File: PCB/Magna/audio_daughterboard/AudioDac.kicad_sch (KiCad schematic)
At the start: 44 parts, among them U401 NE5532, U403 PCM1789

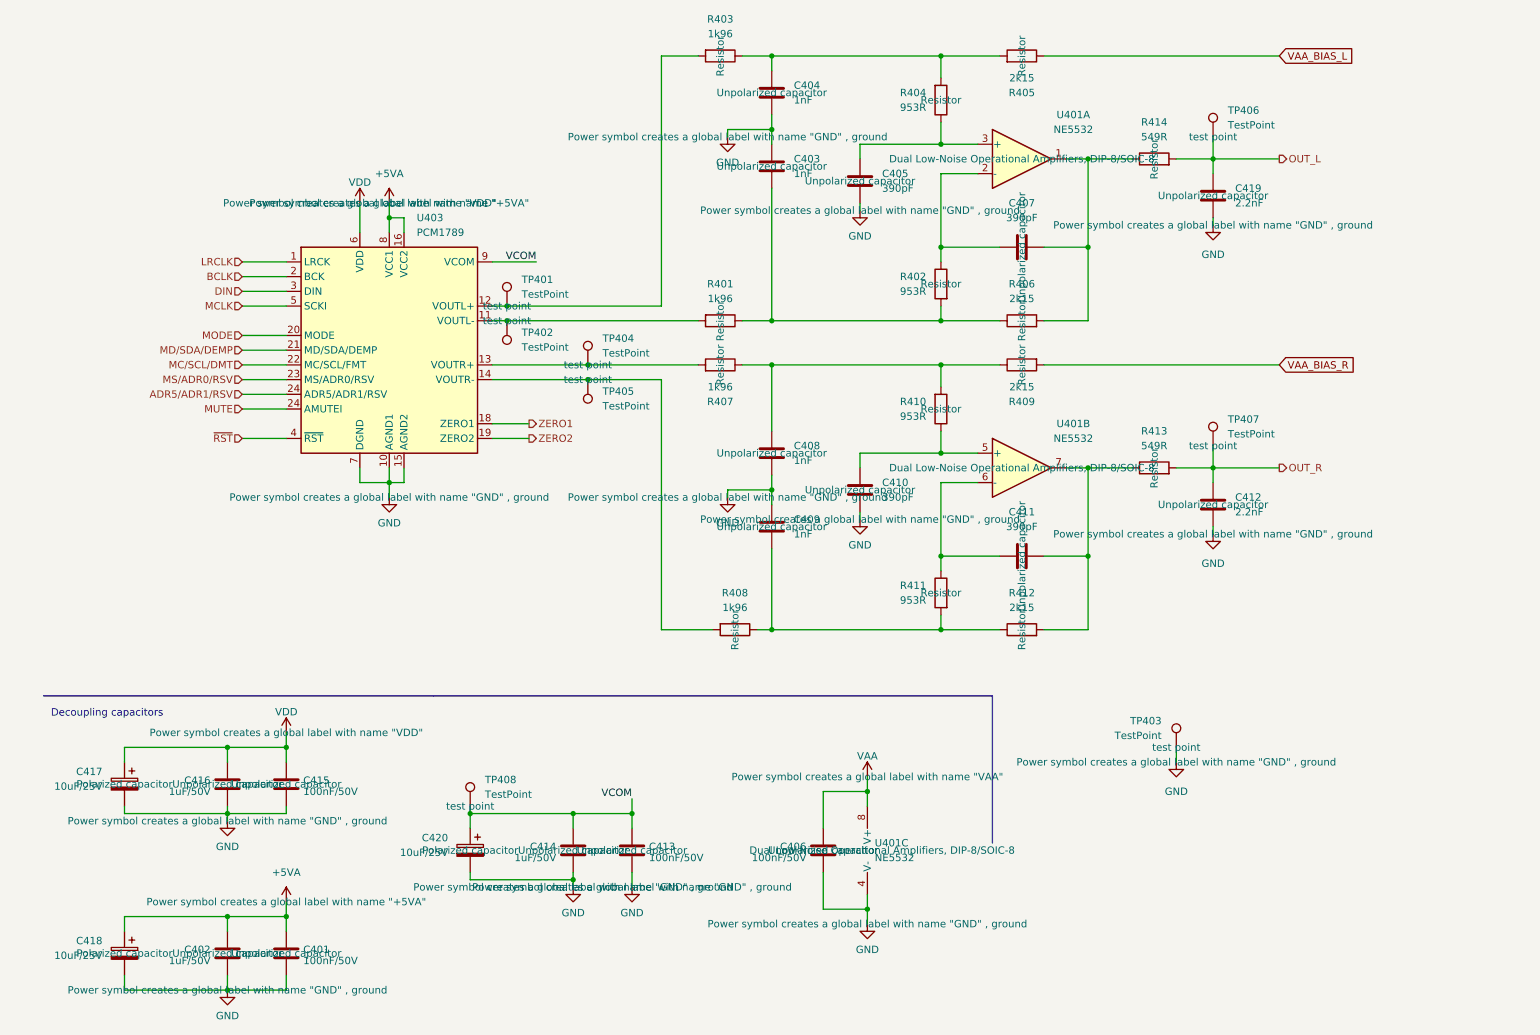
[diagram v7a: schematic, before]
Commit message: Update schematics to Kicad 9
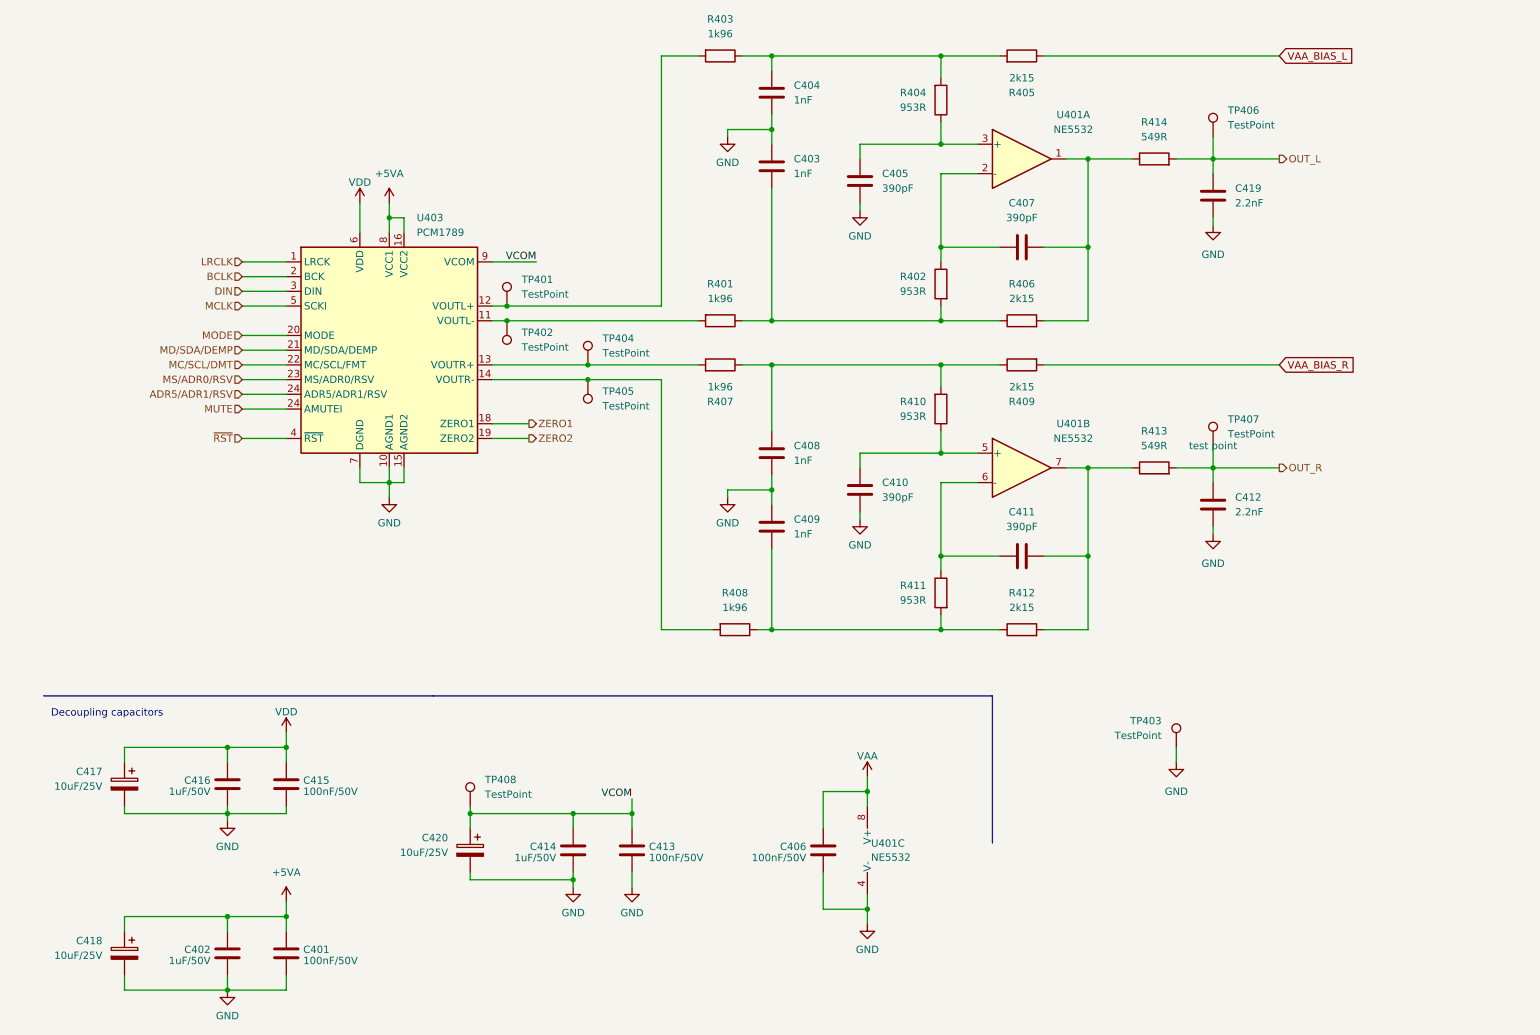
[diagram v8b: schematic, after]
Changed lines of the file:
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@@
 					(size 1.27 1.27)
 				)
+				(hide yes)
 			)
 		)
@@
 					(size 1.27 1.27)
 				)
+				(hide yes)
 			)
 		)
@@
 					(size 1.27 1.27)
 				)
+				(hide yes)
 			)
 		)
@@
 					(size 1.27 1.27)
 				)
+				(hide yes)
 			)
 		)
@@
 					(size 1.27 1.27)
 				)
+				(hide yes)
 			)
 		)
@@
 					(size 1.27 1.27)
 				)
+				(hide yes)
 			)
 		)
@@
 					(size 1.27 1.27)
 				)
+				(hide yes)
 			)
 		)
@@
 					(size 1.27 1.27)
 				)
+				(hide yes)
 			)
 		)
@@
 					(size 1.27 1.27)
 				)
+				(hide yes)
 			)
 		)
@@
 					(size 1.27 1.27)
 				)
+				(hide yes)
 			)
 		)
@@
 					(size 1.27 1.27)
 				)
+				(hide yes)
 			)
 		)
@@
 					(size 1.27 1.27)
 				)
+				(hide yes)
 			)
 		)
@@
 					(size 1.27 1.27)
 				)
+				(hide yes)
 			)
 		)
@@
 					(size 1.27 1.27)
 				)
+				(hide yes)
 			)
 		)
@@
 					(size 1.27 1.27)
 				)
+				(hide yes)
 			)
 		)
@@
 					(size 1.27 1.27)
 				)
+				(hide yes)
 			)
 		)
@@
 					(size 1.27 1.27)
 				)
+				(hide yes)
 			)
 		)
@@
 					(size 1.27 1.27)
 				)
+				(hide yes)
 			)
 		)
@@
 					(size 1.27 1.27)
 				)
+				(hide yes)
 			)
 		)
@@
 					(size 1.27 1.27)
 				)
+				(hide yes)
 			)
 		)
@@
 					(size 1.27 1.27)
 				)
+				(hide yes)
 			)
 		)
@@
 					(size 1.27 1.27)
 				)
+				(hide yes)
 			)
 		)
@@
 					(size 1.27 1.27)
 				)
+				(hide yes)
 			)
 		)
@@
 					(size 1.27 1.27)
 				)
+				(hide yes)
 			)
 		)
@@
 					(size 1.27 1.27)
 				)
+				(hide yes)
 			)
 		)
@@
 					(size 1.27 1.27)
 				)
+				(hide yes)
 			)
 		)
@@
 					(size 1.27 1.27)
 				)
+				(hide yes)
 			)
 		)
@@
 					(size 1.27 1.27)
 				)
+				(hide yes)
 			)
 		)
@@
 		(fields_autoplaced yes)
 		(property "Reference" "U401"
-			(at 156.21 165.1 0)
+			(at 155.575 165.1578 0)
 			(effects
 				(font
@@
 		)
 		(property "Value" "NE5532"
-			(at 156.21 167.64 0)
+			(at 155.575 167.5821 0)
 			(effects
 				(font
@@
 					(size 1.27 1.27)
 				)
+				(hide yes)
 			)
 		)
@@
 				)
 				(path "/1eadd930-2484-4c28-b568-78e6454e7f52/bde964b8-775c-4f2b-9cde-276eb8d923ca"
-					(reference "U503")
+					(reference "U502")
 					(unit 3)
 				)
@@
 					(size 1.27 1.27)
 				)
+				(hide yes)
 			)
 		)
@@
 					(size 1.27 1.27)
 				)
+				(hide yes)
 			)
 		)
@@
 					(size 1.27 1.27)
 				)
+				(hide yes)
 			)
 		)
@@
 					(size 1.27 1.27)
 				)
+				(hide yes)
 			)
 		)
@@
 					(size 1.27 1.27)
 				)
+				(hide yes)
 			)
 		)
@@
 					(size 1.27 1.27)
 				)
+				(hide yes)
 			)
 		)
@@
 					(size 1.27 1.27)
 				)
+				(hide yes)
 			)
 		)
@@
 					(size 1.27 1.27)
 				)
+				(hide yes)
 			)
 		)
@@
 					(size 1.27 1.27)
 				)
+				(hide yes)
 			)
 		)
@@
 					(size 1.27 1.27)
 				)
+				(hide yes)
 			)
 		)
@@
 					(size 1.27 1.27)
 				)
+				(hide yes)
 			)
 		)
@@
 					(size 1.27 1.27)
 				)
+				(hide yes)
 			)
 		)
@@
 					(size 1.27 1.27)
 				)
+				(hide yes)
 			)
 		)
@@
 					(size 1.27 1.27)
 				)
+				(hide yes)
 			)
 		)
@@
 					(size 1.27 1.27)
 				)
+				(hide yes)
 			)
 		)
@@
 					(size 1.27 1.27)
 				)
+				(hide yes)
 			)
 		)
@@
 					(size 1.27 1.27)
 				)
+				(hide yes)
 			)
 		)
@@
 					(size 1.27 1.27)
 				)
+				(hide yes)
 			)
 		)
@@
 					(size 1.27 1.27)
 				)
+				(hide yes)
 			)
 		)
@@
 					(size 1.27 1.27)
 				)
+				(hide yes)
 			)
 		)
@@
 					(size 1.27 1.27)
 				)
+				(hide yes)
 			)
 		)
@@
 					(size 1.27 1.27)
 				)
+				(hide yes)
 			)
 		)
@@
 					(size 1.27 1.27)
 				)
+				(hide yes)
 			)
 		)
@@
 					(size 1.27 1.27)
 				)
+				(hide yes)
 			)
 		)
@@
 					(size 1.27 1.27)
 				)
+				(hide yes)
 			)
 		)
@@
 					(size 1.27 1.27)
 				)
+				(hide yes)
 			)
 		)
@@
 					(size 1.27 1.27)
 				)
+				(hide yes)
 			)
 		)
@@
 					(size 1.27 1.27)
 				)
+				(hide yes)
 			)
 		)
@@
 					(size 1.27 1.27)
 				)
+				(hide yes)
 			)
 		)
@@
 					(size 1.27 1.27)
 				)
+				(hide yes)
 			)
 		)
@@
 					(size 1.27 1.27)
 				)
+				(hide yes)
 			)
 		)
@@
 					(size 1.27 1.27)
 				)
+				(hide yes)
 			)
 		)
@@
 					(size 1.27 1.27)
 				)
+				(hide yes)
 			)
 		)
